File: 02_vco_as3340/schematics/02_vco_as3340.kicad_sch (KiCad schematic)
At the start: 88 parts, among them J1 Conn_02x05_Odd_Even, J10 Triangle Out, J11 Sine Out, J12 1V/O Thru, J2 1V/O IN, J3 Positive Hard Sync IN, J4 Negative Hard Sync IN, J5 Soft Sync In, J6 FM IN, J7 PWM CV IN, J8 Square Out, J9 Sawtooth Out, Q1 2N3904, Q2 2N3904, U1 TL074, U2 AS3340, U3 TL072

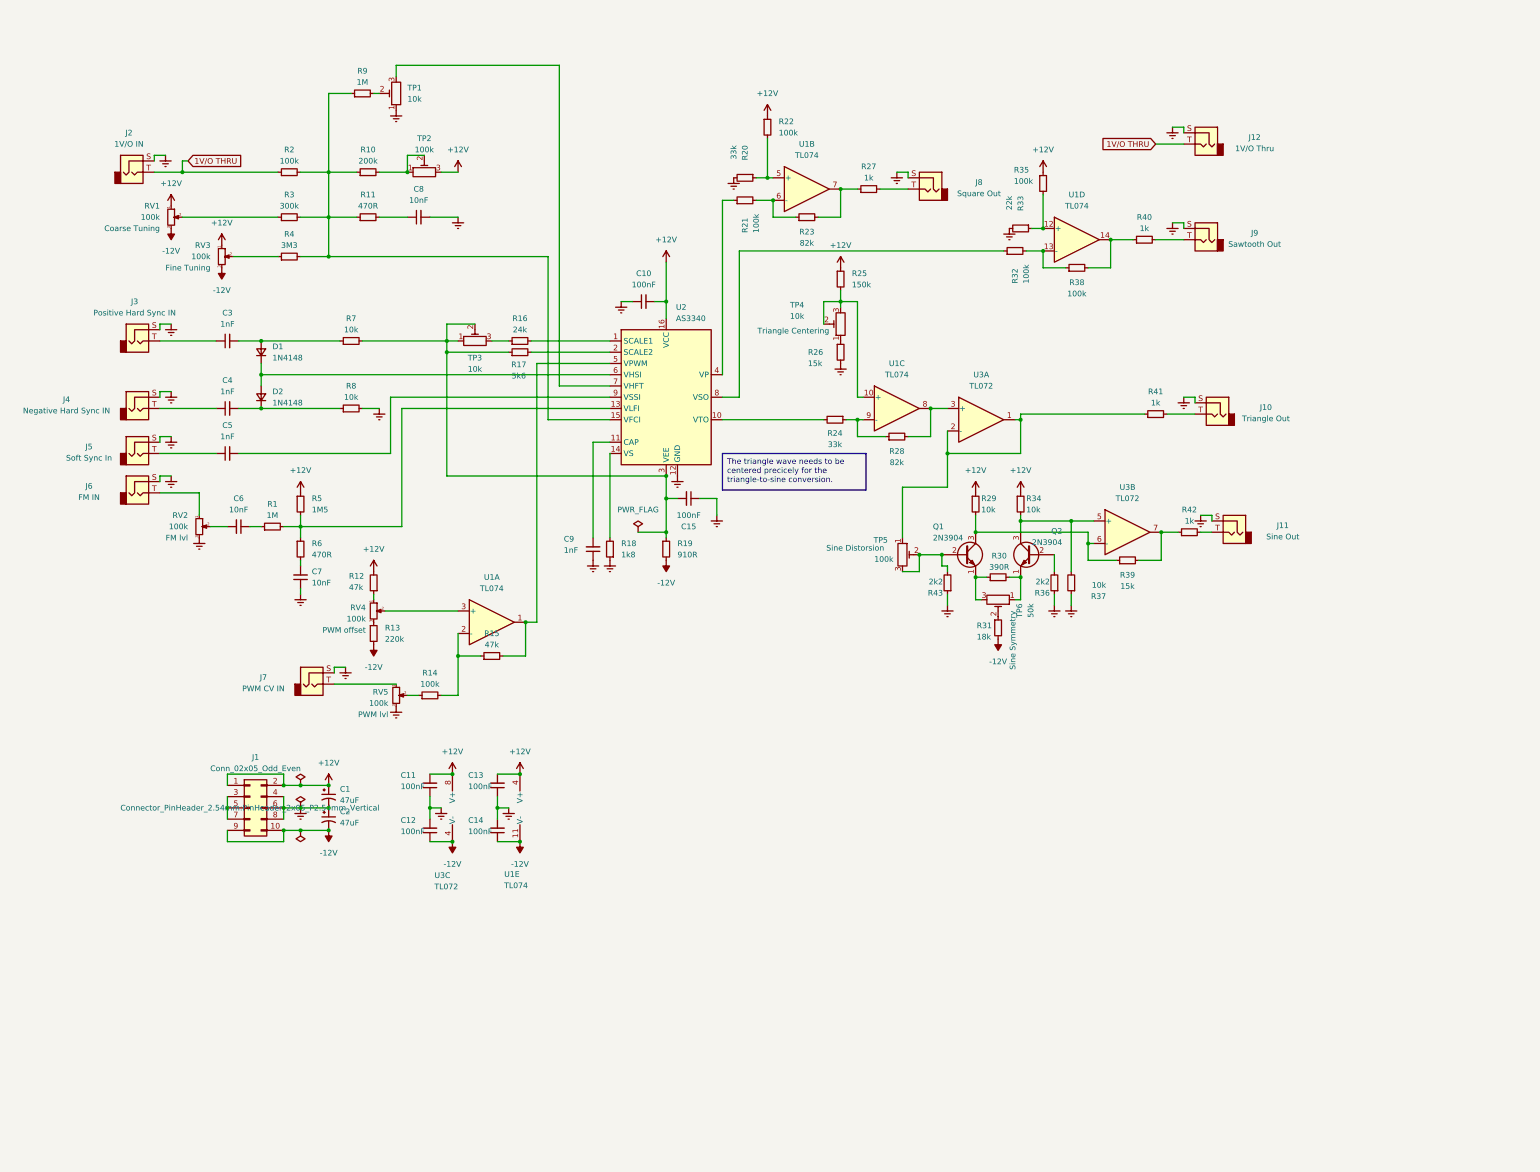
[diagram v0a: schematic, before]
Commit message: fixed triangle output
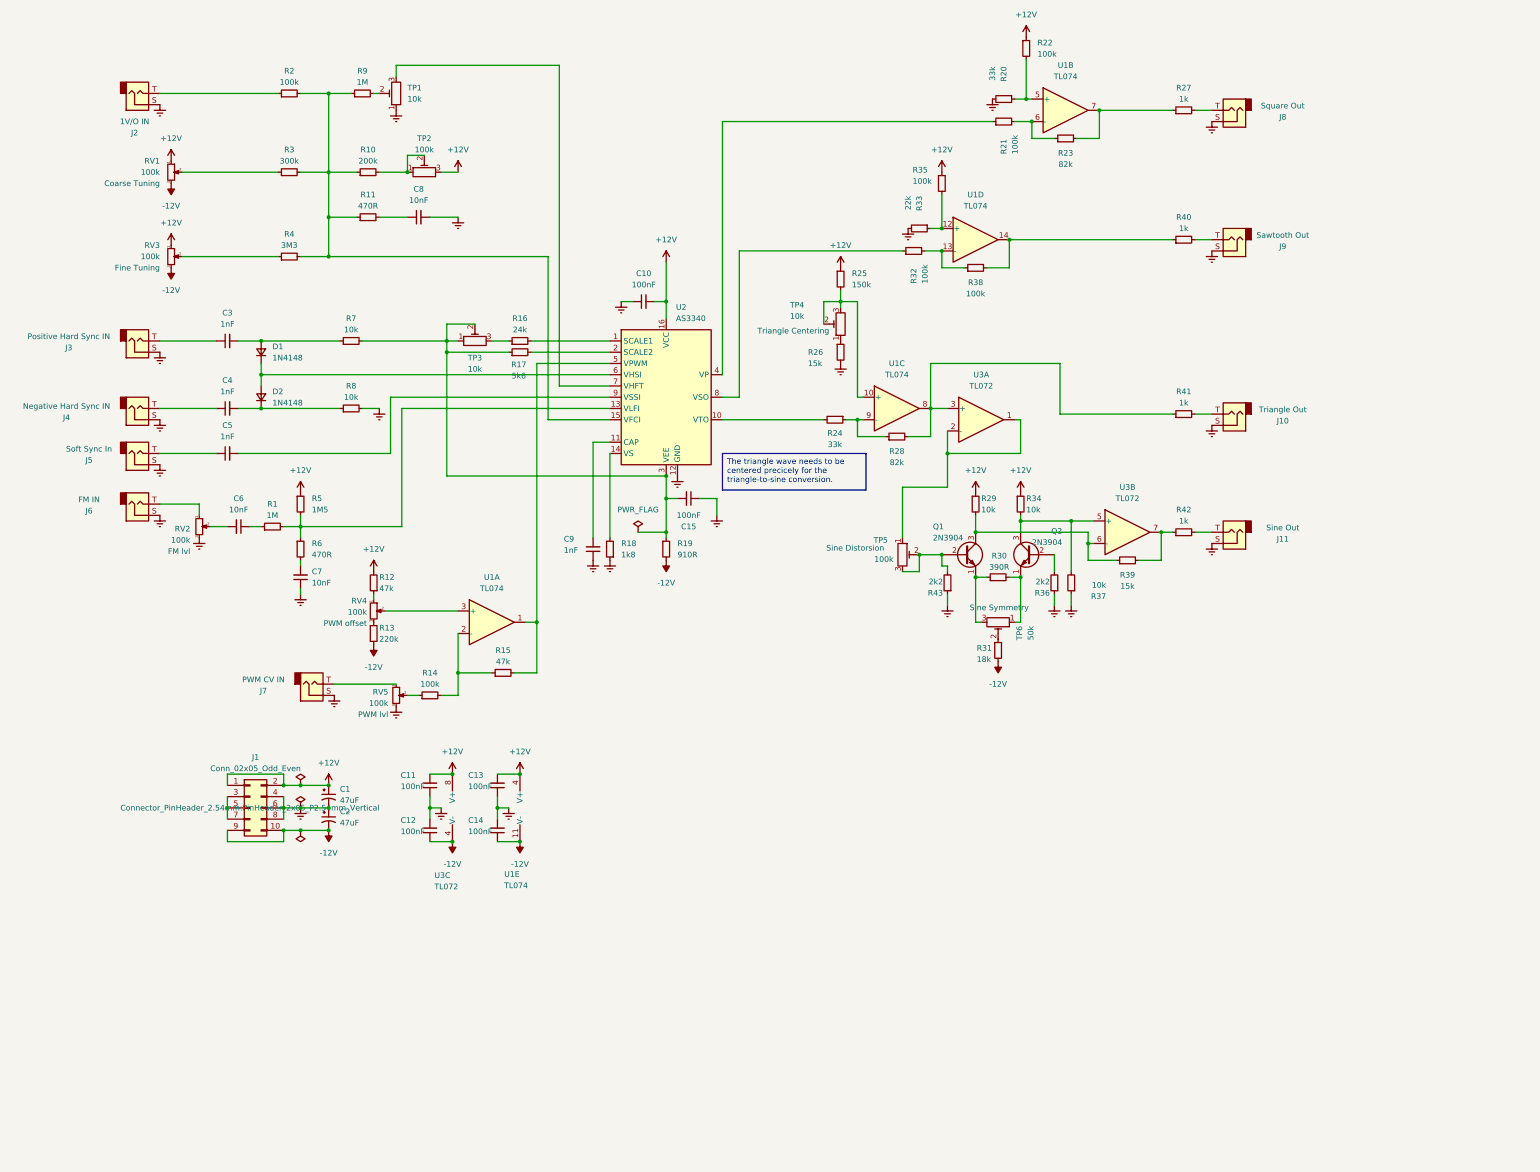
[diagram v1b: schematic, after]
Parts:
- removed J12: 1V/O Thru, Connector_Audio:Jack_6.35mm_Neutrik_NJ5FD-V_Vertical, symbol Connector_Audio:AudioJack2
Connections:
- net at R28.2, U1.8, U3.3 (+): now also R41.1
- net at TP5.1, U3.1, U3.2 (-): no longer R41.1
- net 1V/O THRU: no longer names the net of J2.T, R2.1
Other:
- moved on the sheet: J10, J11, J2, J3, J4, J5, J6, J7, J8, J9, R15, R2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

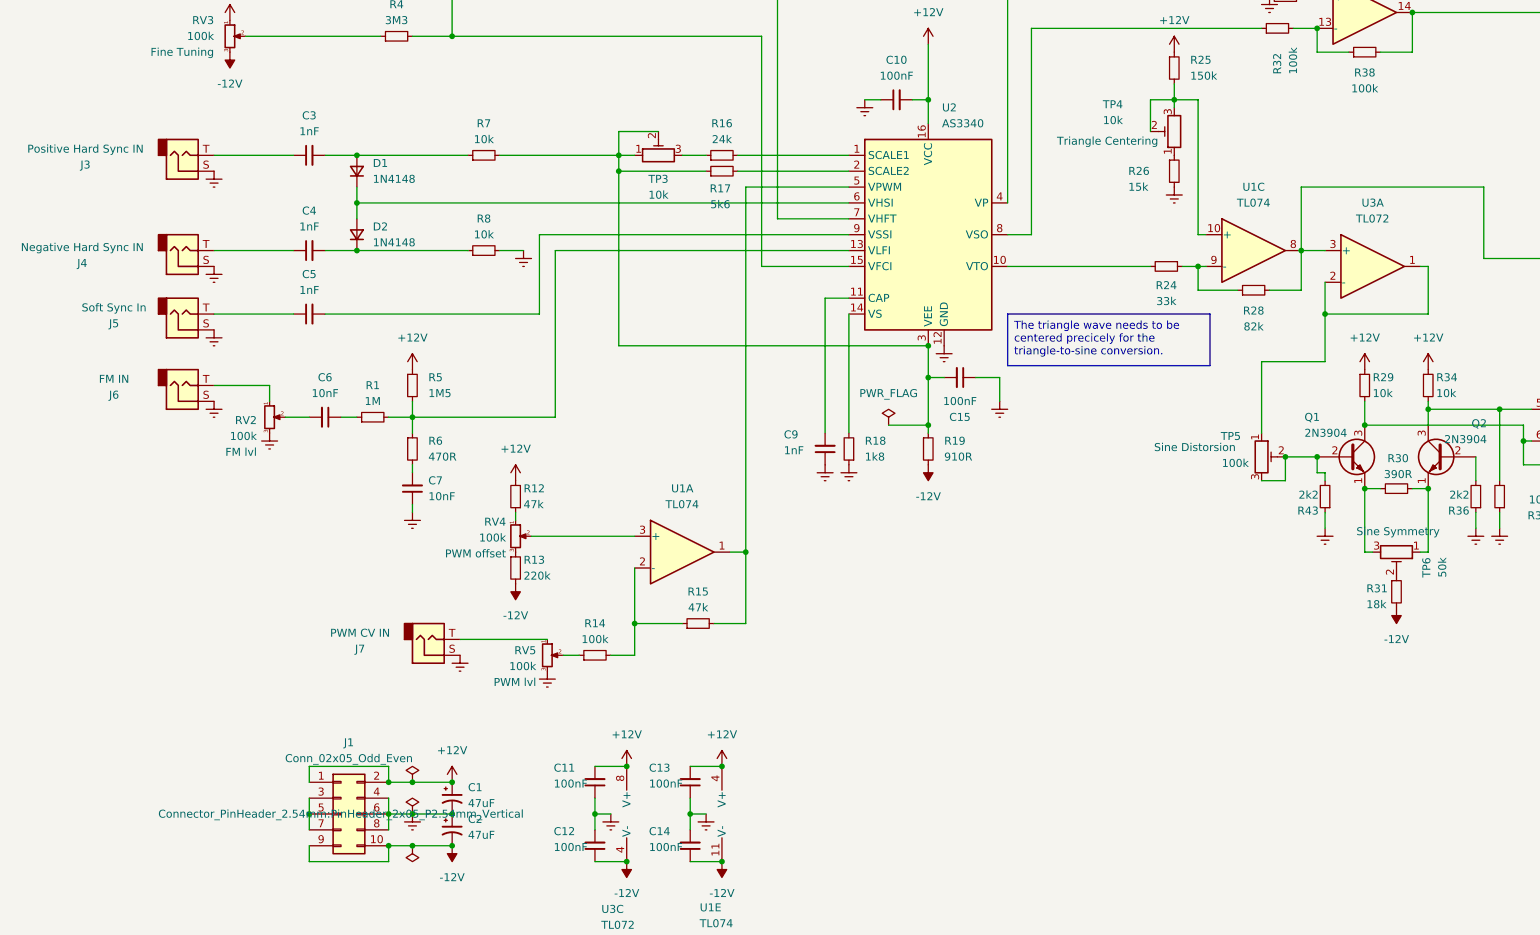
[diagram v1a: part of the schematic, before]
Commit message: added LFO option to 02_vco_as3340
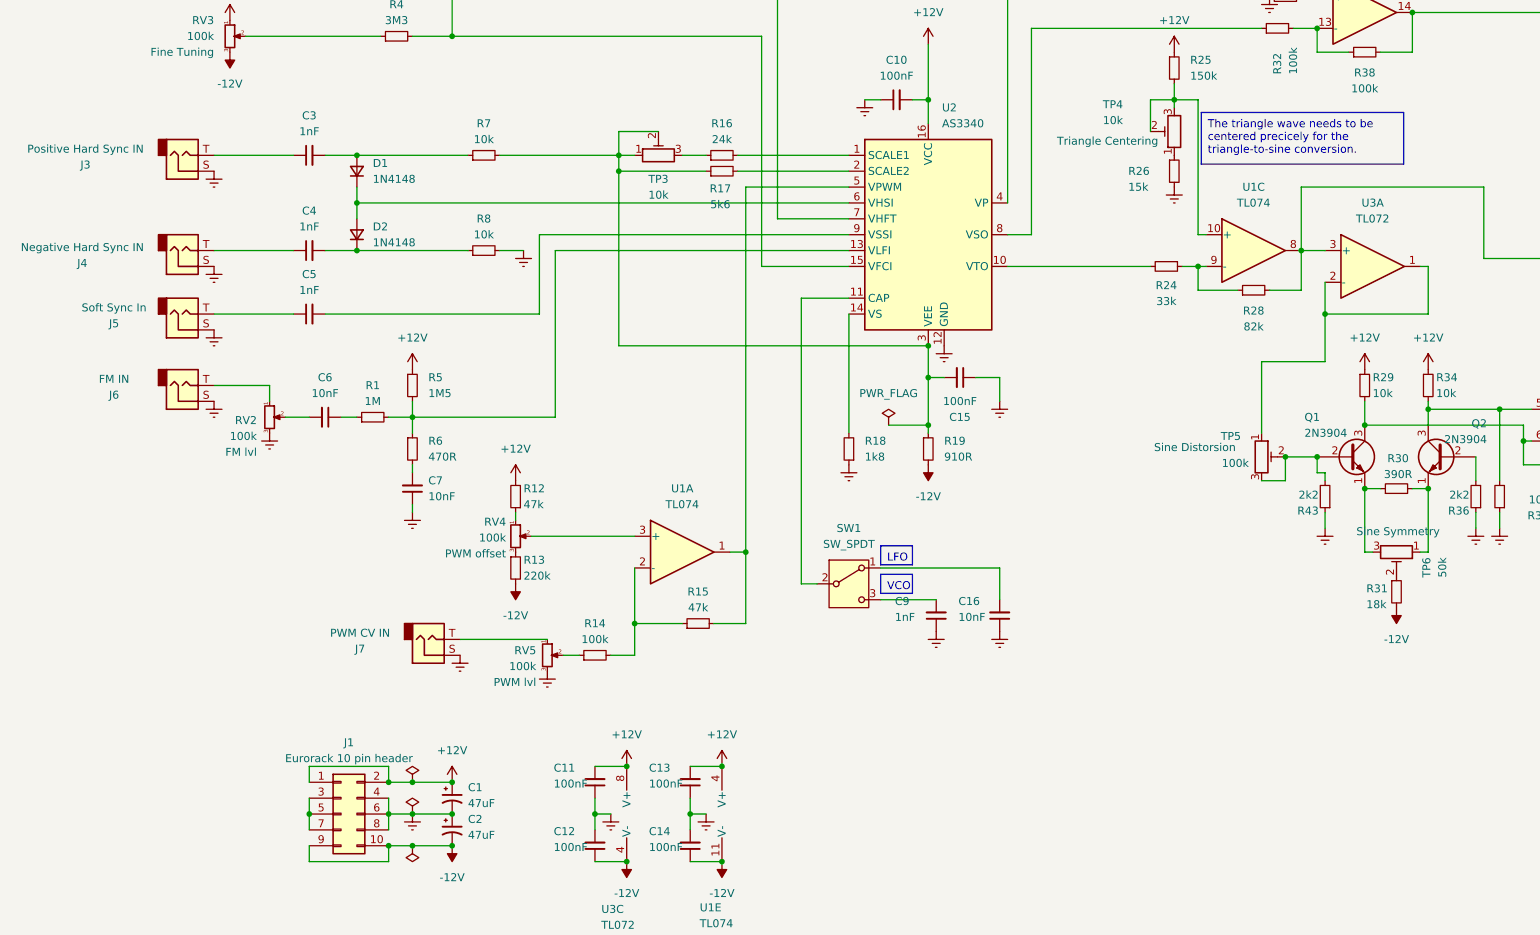
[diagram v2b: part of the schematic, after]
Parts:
- added C16: 10nF, Capacitor_THT:C_Disc_D6.0mm_W2.5mm_P5.00mm, symbol Device:C_Small
- added SW1: SW_SPDT, symbol Switch:SW_SPDT
- J1: value Conn_02x05_Odd_Even -> Eurorack 10 pin header
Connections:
- net GNDREF: now also C16.1
- net at U2.11 (CAP): now also SW1.2 (B); no longer C9.2
- new net: C16.2, SW1.1 (A)
- new net: C9.2, SW1.3 (C)

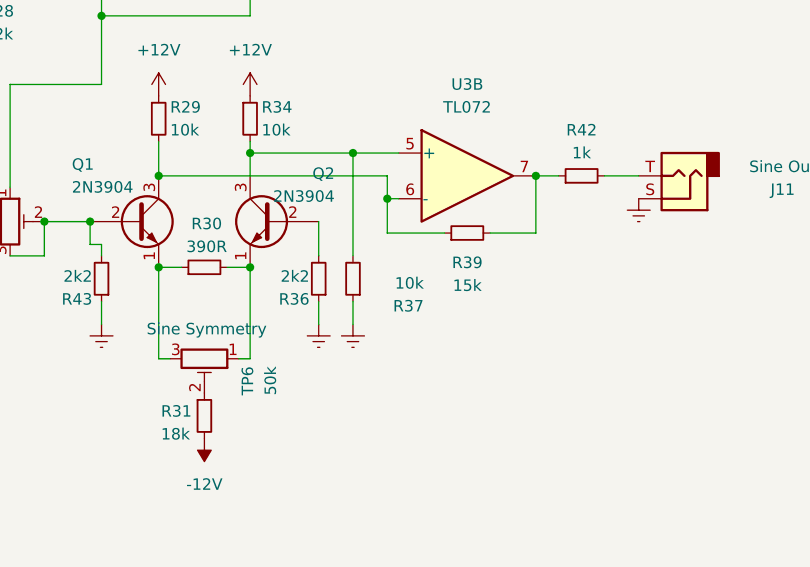
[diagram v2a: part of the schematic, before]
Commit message: corrected R37 to 15k
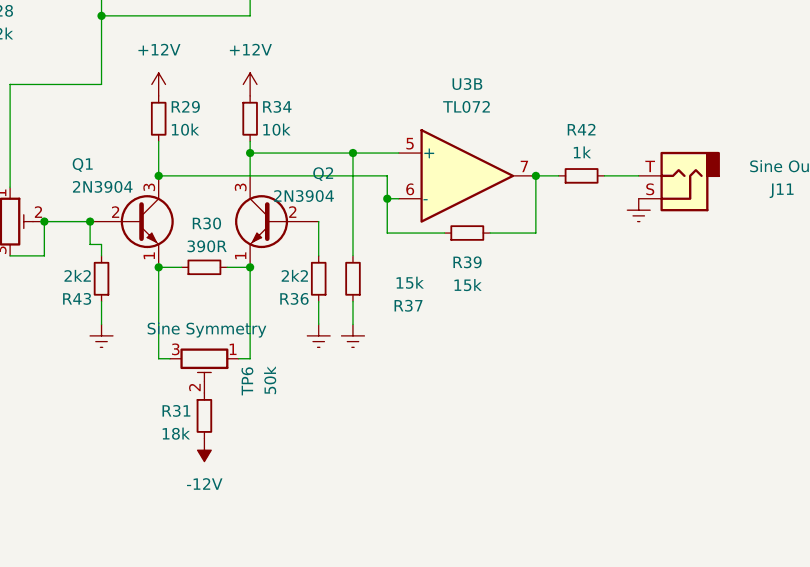
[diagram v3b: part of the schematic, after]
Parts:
- R37: value 10k -> 15k
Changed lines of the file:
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@@
 			)
 		)
-		(property "Value" "10k"
+		(property "Value" "15k"
 			(at 242.824 145.288 0)
 			(effects

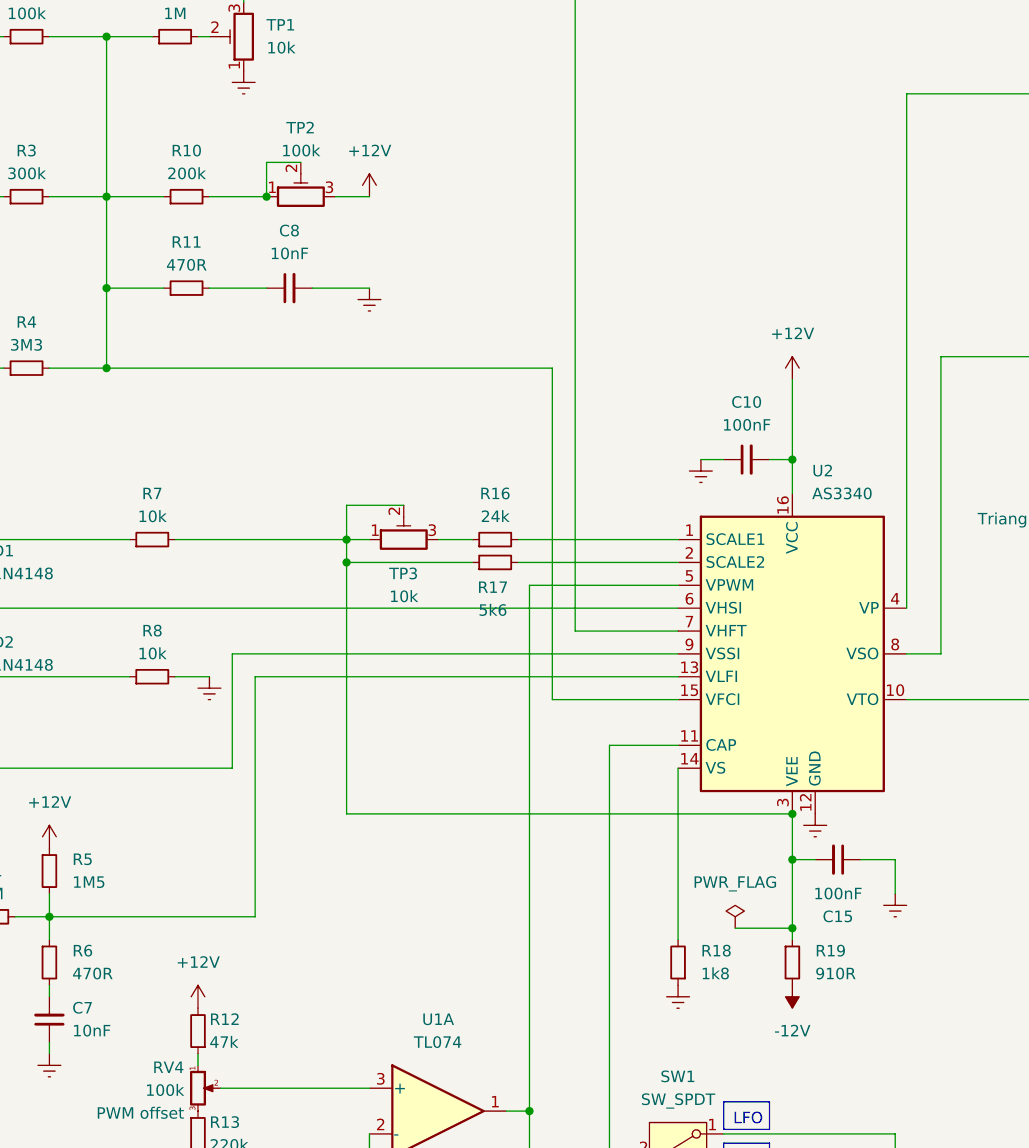
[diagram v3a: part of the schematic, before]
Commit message: fixed some R values for 02_vco
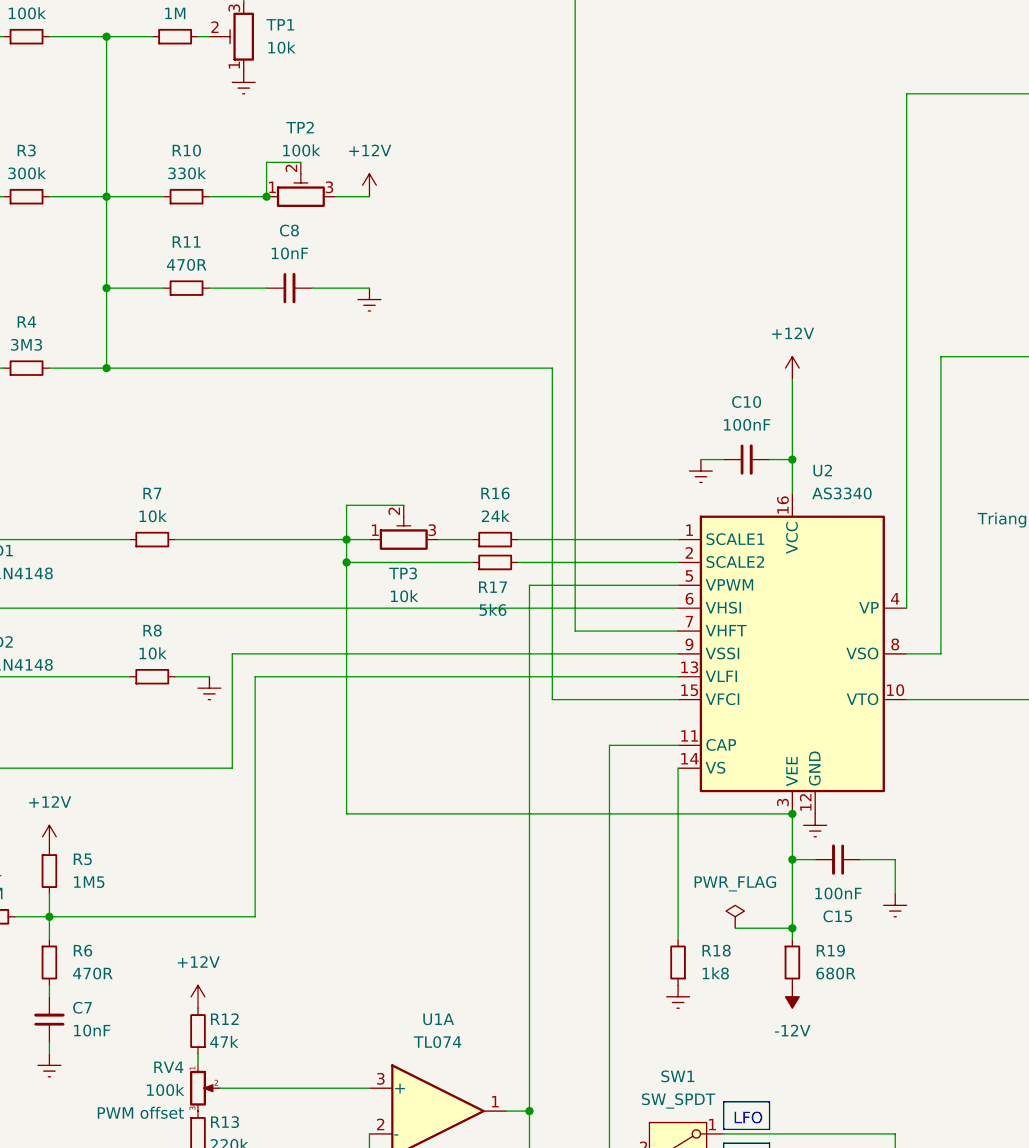
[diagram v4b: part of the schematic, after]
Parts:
- R10: value 200k -> 330k
- R19: value 910R -> 680R
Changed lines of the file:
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@@
 			)
 		)
-		(property "Value" "910R"
+		(property "Value" "680R"
 			(at 146.05 138.4299 0)
 			(effects
@@
 			)
 		)
-		(property "Value" "200k"
+		(property "Value" "330k"
 			(at 76.2 49.53 90)
 			(effects
